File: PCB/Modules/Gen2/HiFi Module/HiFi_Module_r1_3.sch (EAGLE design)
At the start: 19 parts, among them IC1 SN65HVD31DR, IC2 ADUM5200ARWZ, T4_1 TEENSY4.1_FORAUDIO

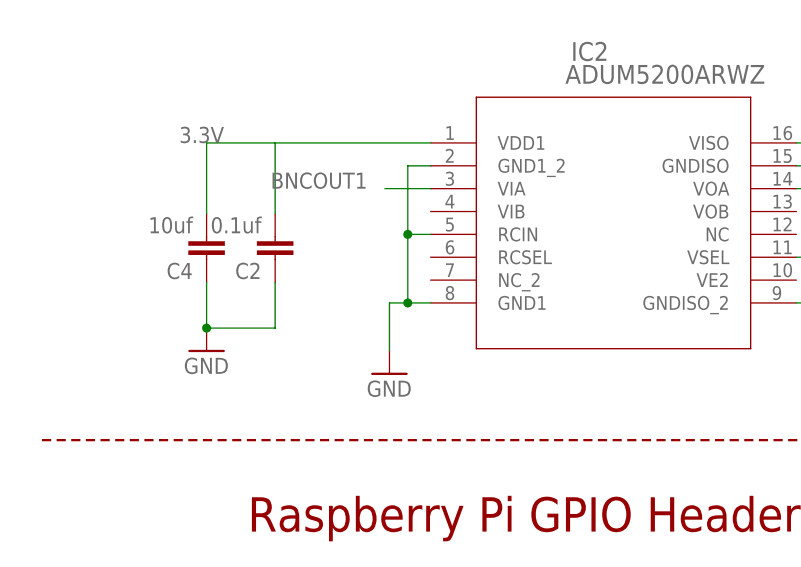
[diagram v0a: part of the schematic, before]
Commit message: -Updated HiFi module PCB to v1.3. New version pulls unused channel to GND on ADUM5200 isolator, and contains silkscreen instructions for header mounting -Updated Raspberry Pi Shim to v1.1. New version provides more space between RJ45 jack and RS-485 IC for even mounting.
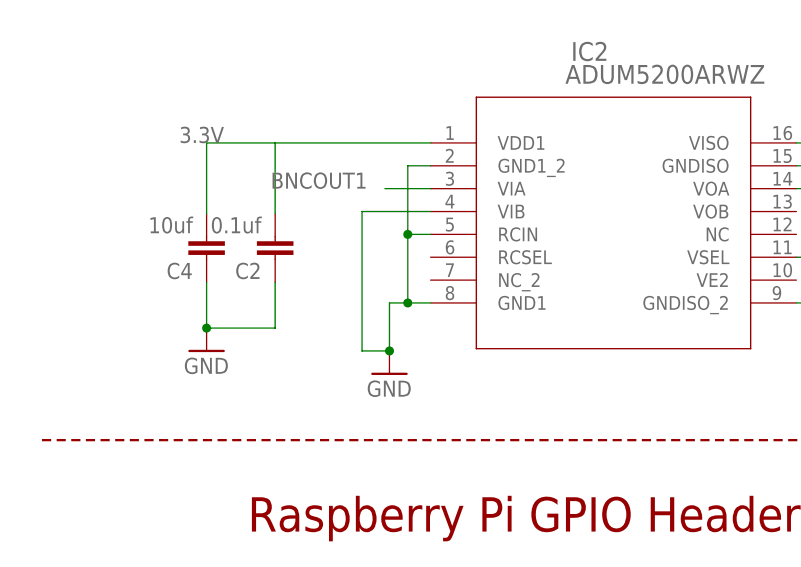
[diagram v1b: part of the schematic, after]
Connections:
- net GND: now also IC2.VIB
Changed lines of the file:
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@@
 <setting verticaltext="up"/>
 </settings>
-<grid distance="0.01" unitdist="inch" unit="inch" style="lines" multiple="1" display="no" altdistance="0.01" altunitdist="inch" altunit="inch"/>
+<grid distance="0.1" unitdist="inch" unit="inch" style="lines" multiple="1" display="no" altdistance="0.01" altunitdist="inch" altunit="inch"/>
 <layers>
 <layer number="1" name="Top" color="4" fill="1" visible="no" active="no"/>
@@
 <wire x1="-12.7" y1="119.38" x2="-15.24" y2="119.38" width="0.1524" layer="91"/>
 <junction x="-15.24" y="119.38"/>
-</segment>
-<segment>
+<pinref part="IC2" gate="A" pin="VIB"/>
+<wire x1="-12.7" y1="121.92" x2="-20.32" y2="121.92" width="0.1524" layer="91"/>
+<wire x1="-20.32" y1="121.92" x2="-20.32" y2="106.426" width="0.1524" layer="91"/>
+<wire x1="-20.32" y1="106.426" x2="-17.272" y2="106.426" width="0.1524" layer="91"/>
+<junction x="-17.272" y="106.426"/>
+</segment>
+<segment>
